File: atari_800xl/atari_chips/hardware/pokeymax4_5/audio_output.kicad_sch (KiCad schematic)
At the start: 22 parts, among them U2 TSV854IQ4T

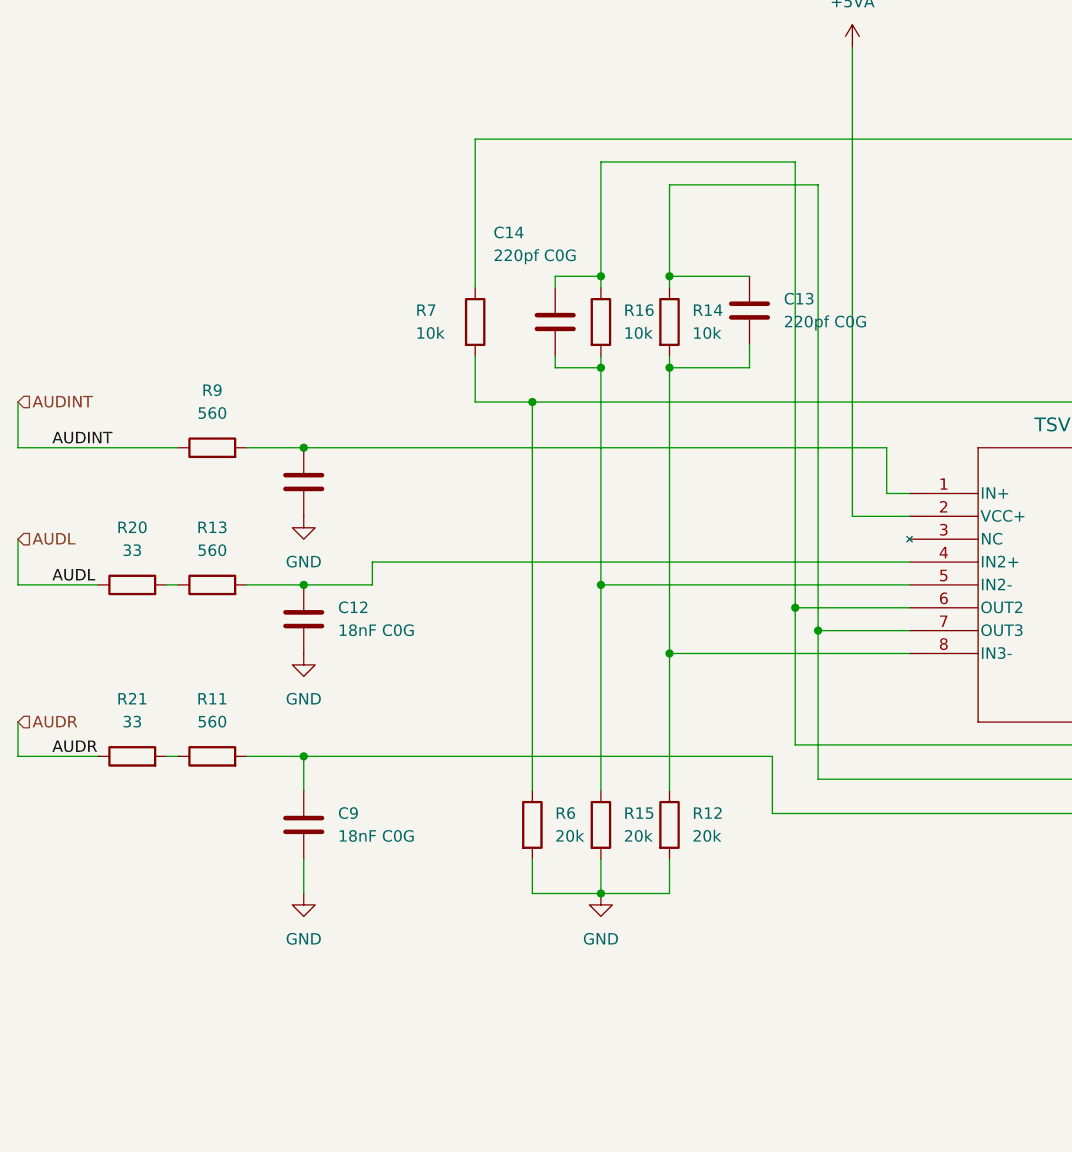
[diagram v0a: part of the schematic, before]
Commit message: Added pokeymax 4.54 (not yet made)
git-svn-id: svn+ssh://192.168.0.3/home/svnfpga/repo/trunk@1559 d6161ac3-aae1-4d52-9b05-ea9ac36b53d3
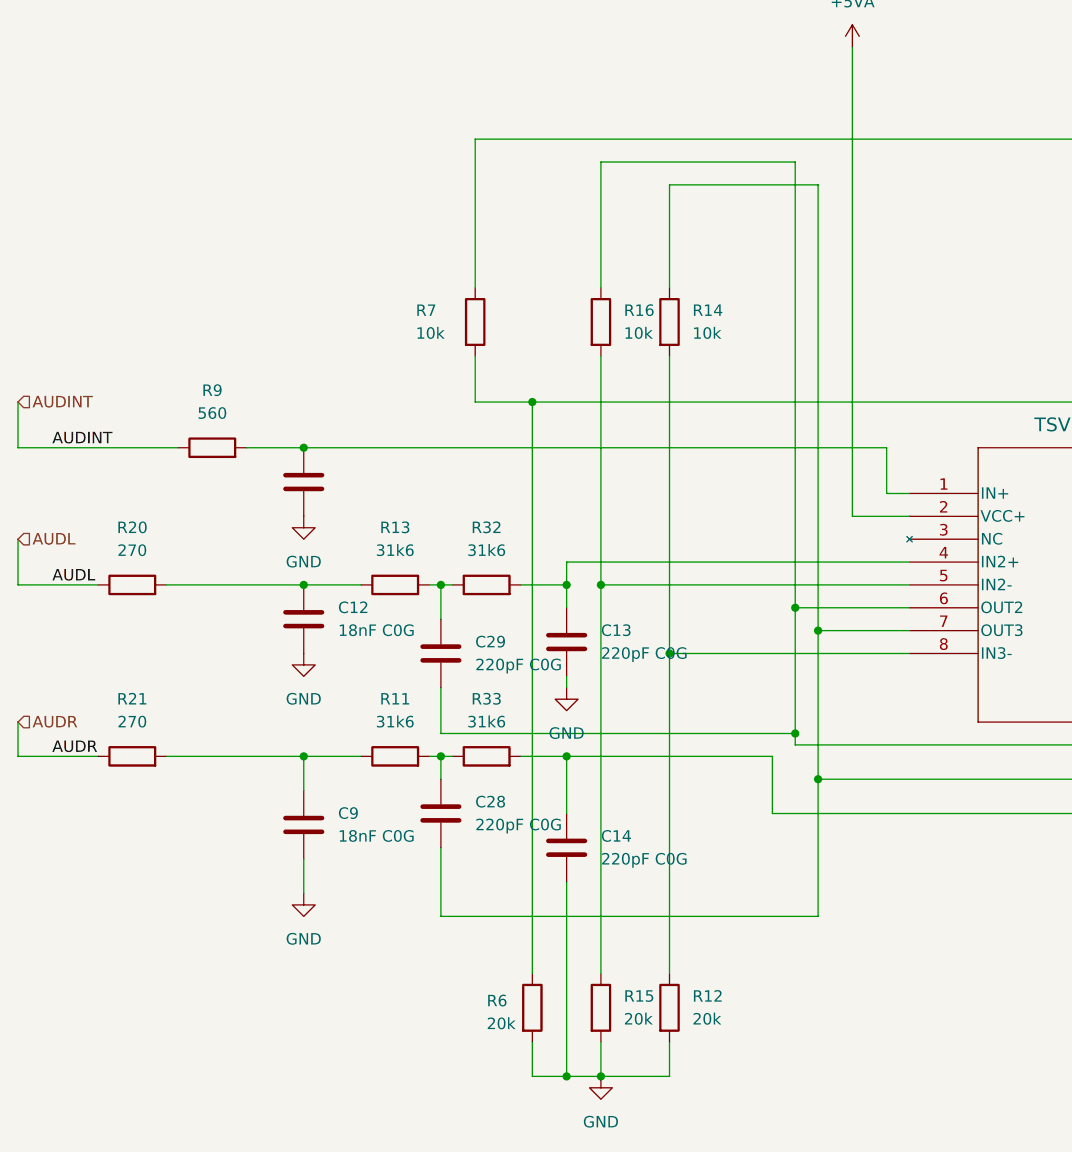
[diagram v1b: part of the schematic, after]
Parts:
- added C28, C29: 220pF C0G, Capacitor_SMD:C_0402_1005Metric, symbol Device:C
- added R32, R33: 31k6, Resistor_SMD:R_0402_1005Metric, symbol Device:R
- C13, C14: value 220pf C0G -> 220pF C0G
- R11, R13: value 560 -> 31k6
- R20, R21: value 33 -> 270
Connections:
- net GND: now also C13.2, C14.2
- net at C7.1, R14.1, U2.7 (OUT3): now also C28.2; no longer C13.1
- net at R12.1, R14.2, U2.8 (IN3-): no longer C13.2
- net at C4.1, R16.1, U2.6 (OUT2): now also C29.2; no longer C14.1
- net at R15.1, R16.2, U2.5 (IN2-): no longer C14.2
- net at R11.1, R21.2: now also C9.1
- net at R13.1, R20.2: now also C12.1
- new net: C29.1, R13.2, R32.1
- new net: C13.1, R32.2, U2.4 (IN2+)
- new net: C14.1, R33.2, U2.9 (IN3+)
- new net: C28.1, R11.2, R33.1
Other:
- moved on the sheet: R11, R12, R13, R15, R6

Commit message: 4.55. Got AI to help me improve a few minor things. Regulator mode, extra decoupling for DAC, distances from edge, gnd/power plane switched, track spacing for a few important lines, bigger cap on 2.5v reg, shorter critical traces on 3.3v reg. Also it double checked the sallen key filter. Switched to the JLCPCB plugin for simpler part management.
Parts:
- C12, C6, C9: LCSC (none) -> C710669
- C13, C14, C28, C29: LCSC (none) -> C71693
- C4, C7: value 2.2uF C0G -> 2.2uF C0G (4.7uF X7R alternative); LCSC (none) -> C5360844
- C8: value 220pf C0G -> 220pF C0G; LCSC (none) -> C71693
- R10, R14, R16, R7: LCSC (none) -> C25744
- R11, R13, R32, R33: LCSC (none) -> C11463
- R12, R15, R6: LCSC (none) -> C25765
- R20, R21: LCSC (none) -> C163474
- R8: LCSC (none) -> C166559
- R9: LCSC (none) -> C163460
- U2: LCSC (none) -> C2058240
